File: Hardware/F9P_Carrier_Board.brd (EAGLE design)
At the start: 56.9 x 66 mm, 170 parts, among them J4 U.FL, J5 QWIIC_RIGHT_ANGLE, J6 MICROMOD-2222-C, J8 JTAG, U1 U-BLOX_ZED-F9P, U5 AP7361C-33

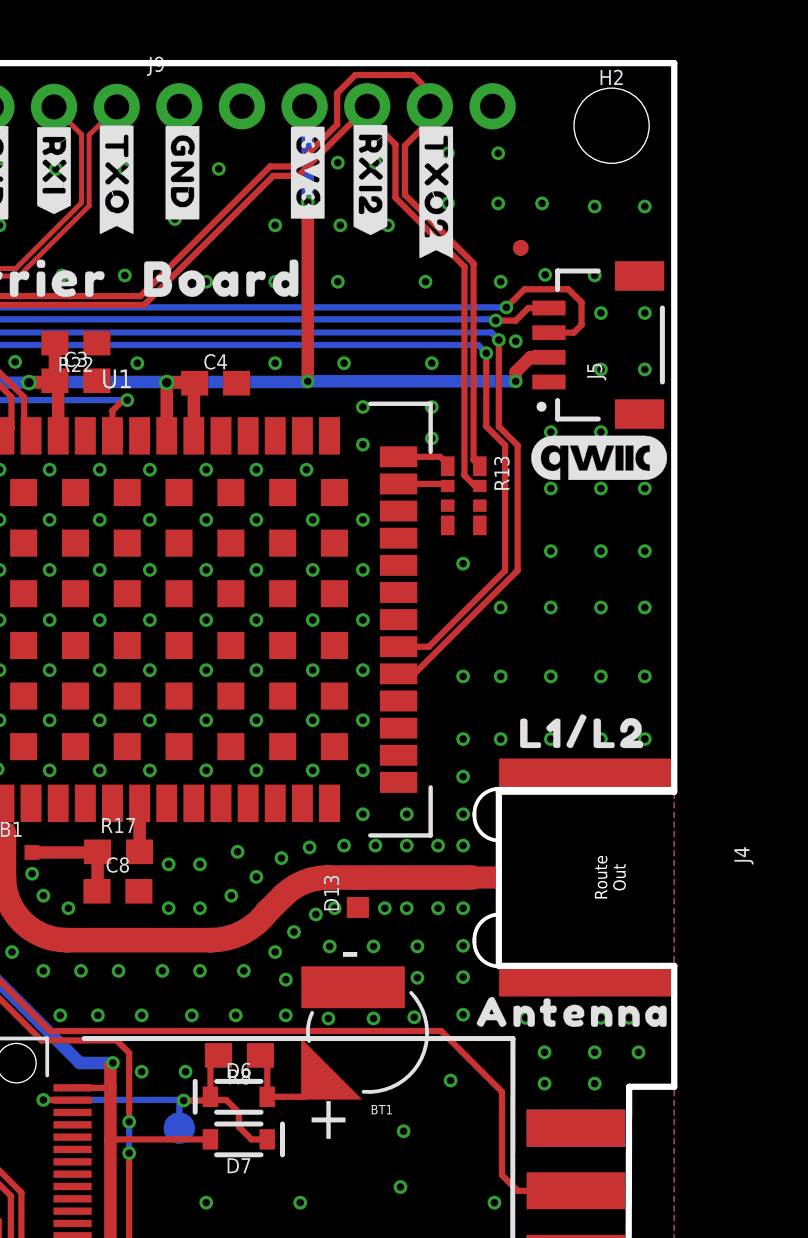
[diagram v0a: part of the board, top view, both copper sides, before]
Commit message: Replaces SMD SMA connector with PTH one
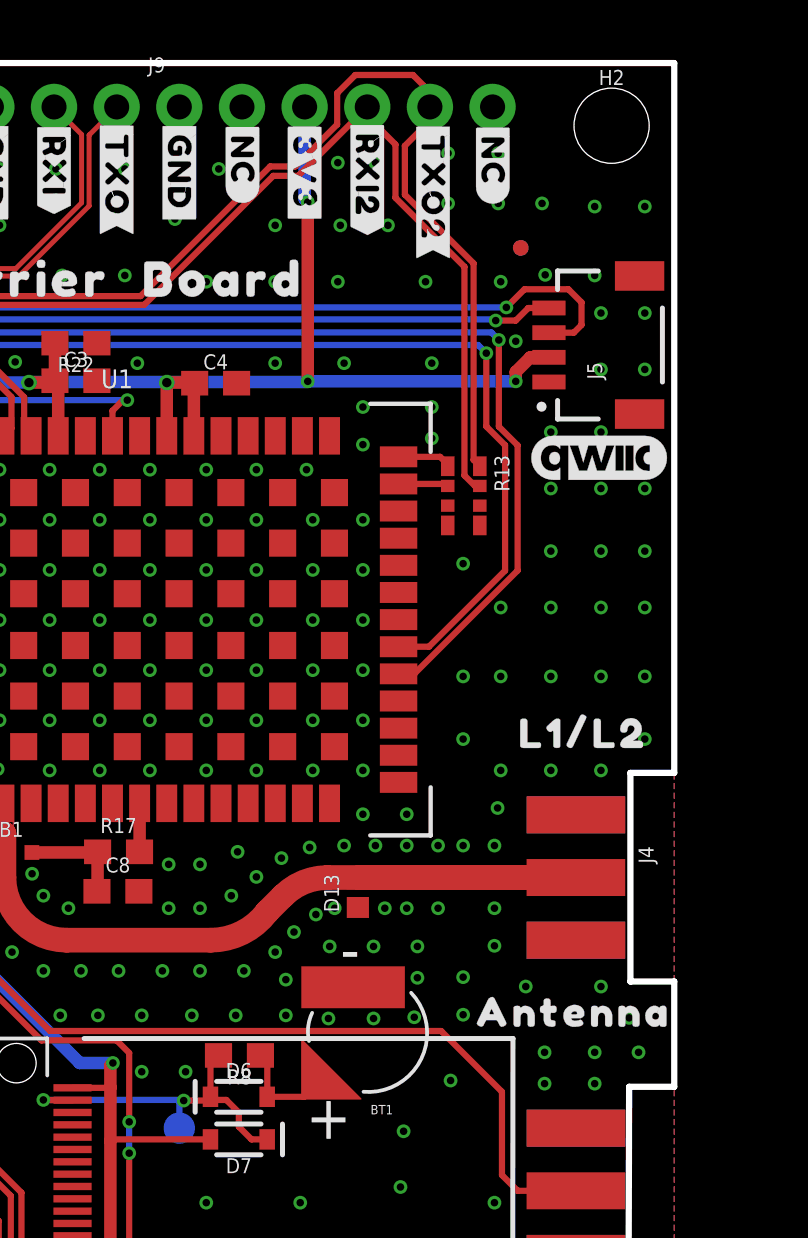
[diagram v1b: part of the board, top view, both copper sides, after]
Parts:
- added U$55, U$83: (no value), top:#NC#4
- added U$84, U$85: (no value), top:#NC#5
- J4: device SparkFun-RF:SMA-EDGE-SMD -> SparkFun-RF:SMA-EDGE
- moved J4 3.89 mm to (52.9, 33.0)
- moved U$15 0.13 mm to (47.1, 61.0)
- moved U$3 0.13 mm to (41.9, 61.6)
- moved U$32 0.13 mm to (41.9, 61.6)
- moved U$33 0.13 mm to (36.8, 61.6)
- moved U$38 0.13 mm to (47.1, 61.0)
- moved U$7 0.13 mm to (36.8, 61.6)
- moved U$11 0.13 mm to (44.5, 61.5)
- moved U$40 0.13 mm to (44.5, 61.5)
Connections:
- net GND: now also J4.GND@2, J4.GND@3
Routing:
- net RF_IN: track 22.5 -> 35.5 mm
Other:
- outline, holes or cut-outs redrawn
